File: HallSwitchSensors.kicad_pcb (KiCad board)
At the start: 2 copper layers, 33 x 33 mm, 28 parts, among them K1 CONN_3, K2 CONN_3, K3 CONN_3, K4 CONN_3

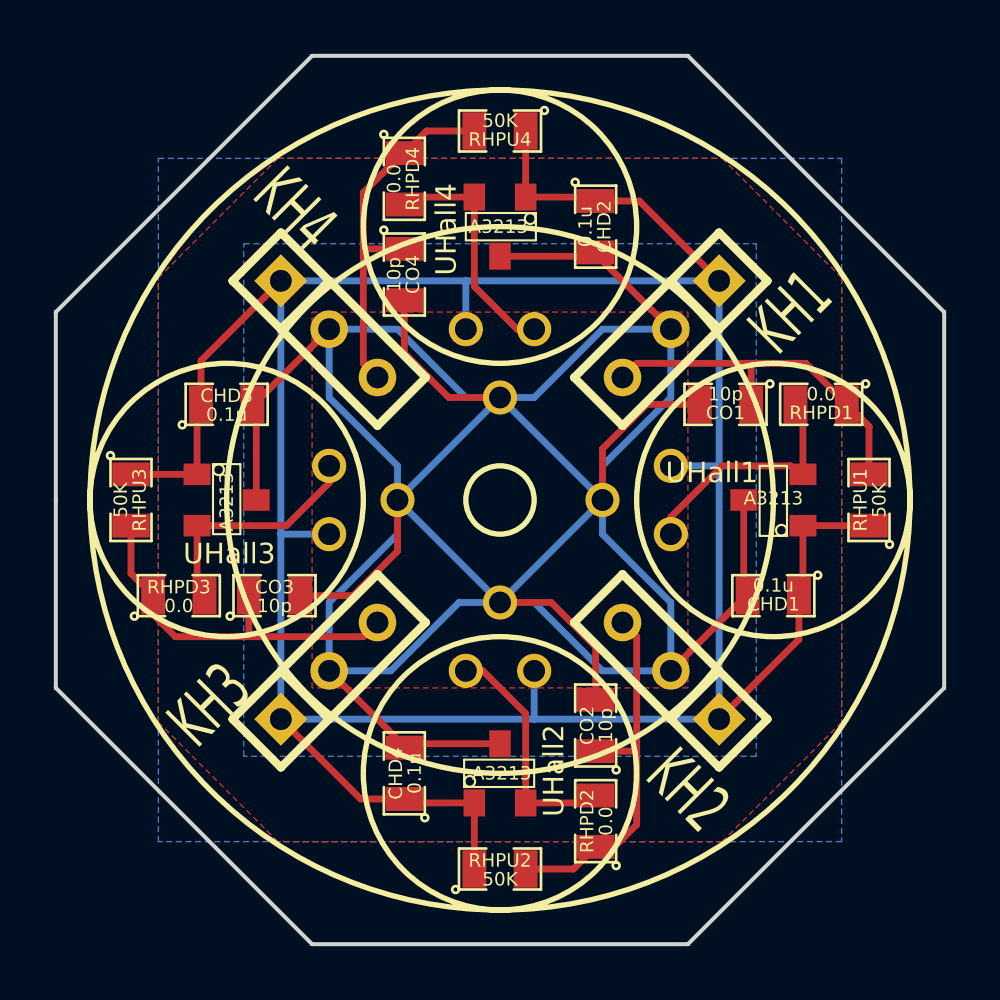
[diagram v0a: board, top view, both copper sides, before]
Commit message: Fixed up fill using Windows version of KiCAD
Fewer crashing in Windows version of KiCAD getting copper fill to
behave.  Now to try again on MacOSX based on what I know here.
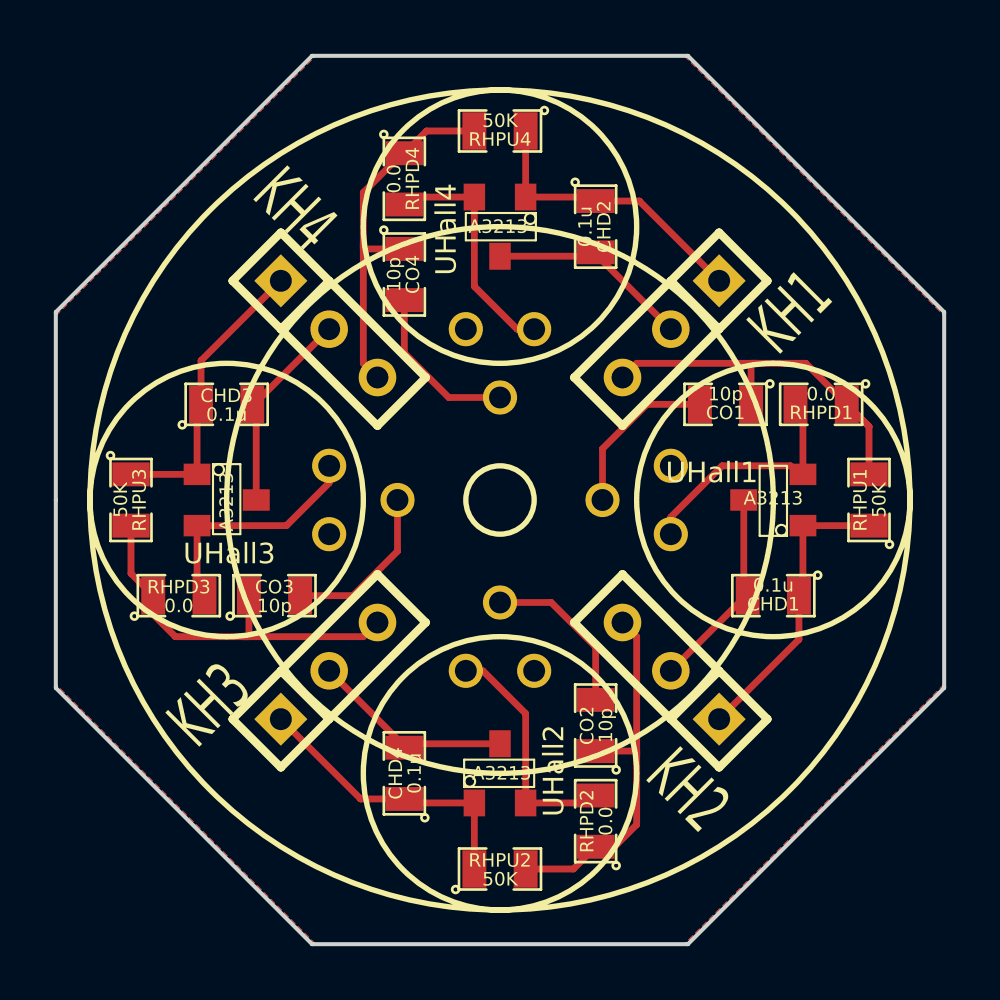
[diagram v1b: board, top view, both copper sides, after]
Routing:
- net GND: track 136.1 -> 55.4 mm
- net +5V: track 116.3 -> 43.8 mm
- removed copper zone on F.Cu, net +5V
- removed copper zone on B.Cu, net GND
